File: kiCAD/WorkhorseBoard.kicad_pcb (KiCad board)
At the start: 4 copper layers, 205 x 97 mm, 384 parts, among them J1 USB_B_Mini, J10 MAIN_POWER, J11 BED_POWER, J12 H0, J13 F0, J15 F1, J16 F4, J17 H1, J19 F2, J2 Micro_SD_Card, J20 F5, J21 H2, J22 F3, J23 HB, J24 Conn_01x02, J25 Conn_01x02, J26 Conn_01x02, J27 Conn_01x02, J28 Conn_01x03, J29 Conn_01x03, J3 Conn_01x06, J30 Conn_01x03, J31 Conn_01x03, J32 Conn_01x03, J33 Conn_01x03, J4 X, J5 E0, J6 Y, J7 E1, J8 Z, J9 E2, Q1 Q_NMOS_GSD, Q10 Q_NMOS_GDS, Q2 Q_NMOS_GDS, Q3 Q_NMOS_GSD, Q4 Q_NMOS_GSD, Q5 Q_NMOS_GDS, Q6 Q_NMOS_GSD, Q7 Q_NMOS_GSD, Q8 Q_NMOS_GDS, Q9 Q_NMOS_GSD, SW1 SW_Push, U1 24C02, U10 TPS54531, U11 TPS54531, U12 AP7361C-33E-13, U13 74HCT365, U14 74HCT365, U2 USBLC6-2SC6, U3 STM32F446VETx, U4 TMC2209, U5 TMC2209, U6 TMC2209, U7 TMC2209, U8 TMC2209, U9 TMC2209, Y1 X322512MSB4SI

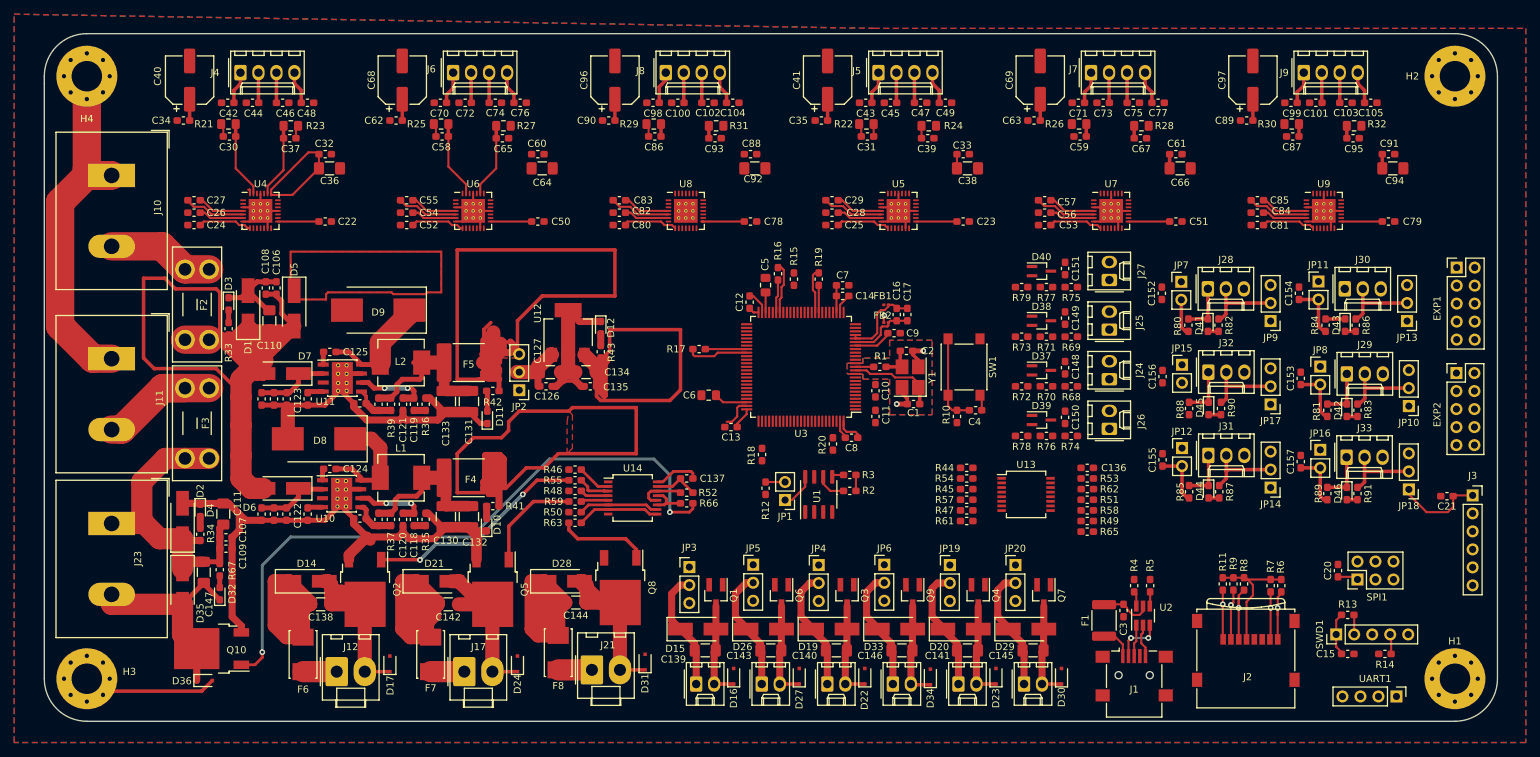
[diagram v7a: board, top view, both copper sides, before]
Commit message: added power plane
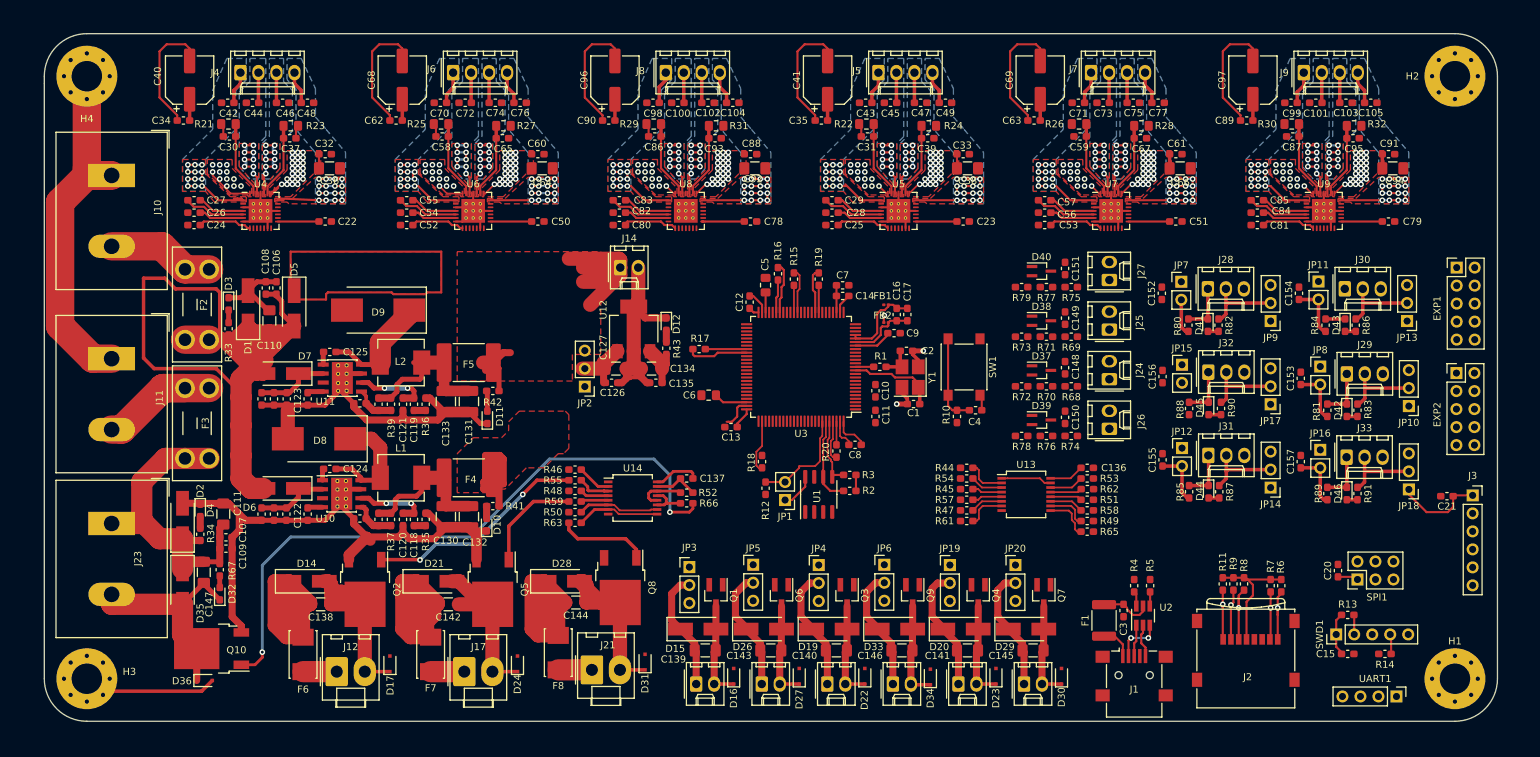
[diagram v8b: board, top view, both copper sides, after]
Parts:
- added J14: 5V_EXT, Connector_Molex:Molex_KK-254_AE-6410-02A_1x02_P2.54mm_Vertical, F.Cu at (107.2, 62.0)
- moved C126 9.26 mm to (106.0, 78.2)
- moved C127 9.26 mm to (106.6, 76.2)
- moved C134 9.26 mm to (111.7, 76.2)
- moved C135 9.26 mm to (112.3, 78.2)
- moved D12 9.26 mm to (113.8, 70.0)
- moved JP2 9.26 mm to (102.2, 78.8)
- moved R43 9.26 mm to (113.8, 73.4)
- moved U12 9.26 mm to (109.2, 70.7)
- moved C8 1.12 mm to (140.4, 87.0)
- moved R20 1.12 mm to (137.8, 87.9)
- moved R18 1.00 mm to (127.2, 89.4)
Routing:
- net GND: track 358.9 -> 478.0 mm
- net +5V: track 134.1 -> 62.3 mm
- net +12V: track 87.0 -> 20.2 mm
- net +3V3: track 138.5 -> 93.5 mm
- net X_OA2: track 4.65 -> 27.4 mm, vias 0 -> 16
- net E2_OA2: track 4.65 -> 26.4 mm, vias 0 -> 16
- net E1_OA2: track 4.65 -> 26.4 mm, vias 0 -> 16
- net E0_OA2: track 4.65 -> 26.4 mm, vias 0 -> 16
- net Z_OA2: track 4.65 -> 26.4 mm, vias 0 -> 16
- net Y_OA2: track 4.65 -> 26.4 mm, vias 0 -> 16
- net X_OB2: track 4.63 -> 23.7 mm, vias 0 -> 12
- net Y_OB2: track 4.63 -> 22.8 mm, vias 0 -> 12
- net E0_OB2: track 4.63 -> 22.5 mm, vias 0 -> 12
- net E2_OB2: track 4.63 -> 22.4 mm, vias 0 -> 12
- net E1_OB2: track 4.63 -> 22.3 mm, vias 0 -> 12
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- added copper zone on In2.Cu, net +12V
- added copper zone on In2.Cu, net +24V
- added copper zone on In2.Cu, net +3V3
- added copper zone on In2.Cu, net +5V
- added copper zone on B.Cu, net E0_OA1
- added copper zone on F.Cu, net E0_OA1
- added copper zone on B.Cu, net E0_OA2
- added copper zone on F.Cu, net E0_OA2
- added copper zone on B.Cu, net E0_OB1
- added copper zone on F.Cu, net E0_OB1
- added copper zone on B.Cu, net E0_OB2
- added copper zone on F.Cu, net E0_OB2
- added copper zone on B.Cu, net E1_OA1
- added copper zone on F.Cu, net E1_OA1
- added copper zone on B.Cu, net E1_OA2
- added copper zone on F.Cu, net E1_OA2
- added copper zone on B.Cu, net E1_OB1
- added copper zone on F.Cu, net E1_OB1
- added copper zone on B.Cu, net E1_OB2
- added copper zone on F.Cu, net E1_OB2
- added copper zone on B.Cu, net E2_OA1
- added copper zone on F.Cu, net E2_OA1
- added copper zone on B.Cu, net E2_OA2
- added copper zone on F.Cu, net E2_OA2
- added copper zone on B.Cu, net E2_OB1
- added copper zone on F.Cu, net E2_OB1
- added copper zone on B.Cu, net E2_OB2
- added copper zone on F.Cu, net E2_OB2
- added copper zone on In2.Cu, net VM
- added copper zone on B.Cu, net X_OA1
- added copper zone on F.Cu, net X_OA1
- added copper zone on B.Cu, net X_OA2
- added copper zone on F.Cu, net X_OA2
- added copper zone on B.Cu, net X_OB1
- added copper zone on F.Cu, net X_OB1
- added copper zone on B.Cu, net X_OB2
- added copper zone on F.Cu, net X_OB2
- added copper zone on B.Cu, net Y_OA1
- added copper zone on F.Cu, net Y_OA1
- added copper zone on B.Cu, net Y_OA2
- added copper zone on F.Cu, net Y_OA2
- added copper zone on B.Cu, net Y_OB1
- added copper zone on F.Cu, net Y_OB1
- added copper zone on B.Cu, net Y_OB2
- added copper zone on F.Cu, net Y_OB2
- added copper zone on B.Cu, net Z_OA1
- added copper zone on F.Cu, net Z_OA1
- added copper zone on B.Cu, net Z_OA2
- added copper zone on F.Cu, net Z_OA2
- added copper zone on B.Cu, net Z_OB1
- added copper zone on F.Cu, net Z_OB1
- added copper zone on B.Cu, net Z_OB2
- added copper zone on F.Cu, net Z_OB2
- removed copper zone on F.Cu, net +3V3
- removed copper zone on B.Cu, net GND
- removed copper zone on F.Cu, net GND
